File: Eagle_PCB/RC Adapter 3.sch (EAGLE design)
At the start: 20 parts, among them IC1 DRV8833, IC2 DRV8833, IC3 ARDUINO_PRO_MICRO, X1 MKDSN1,5/2-5,08

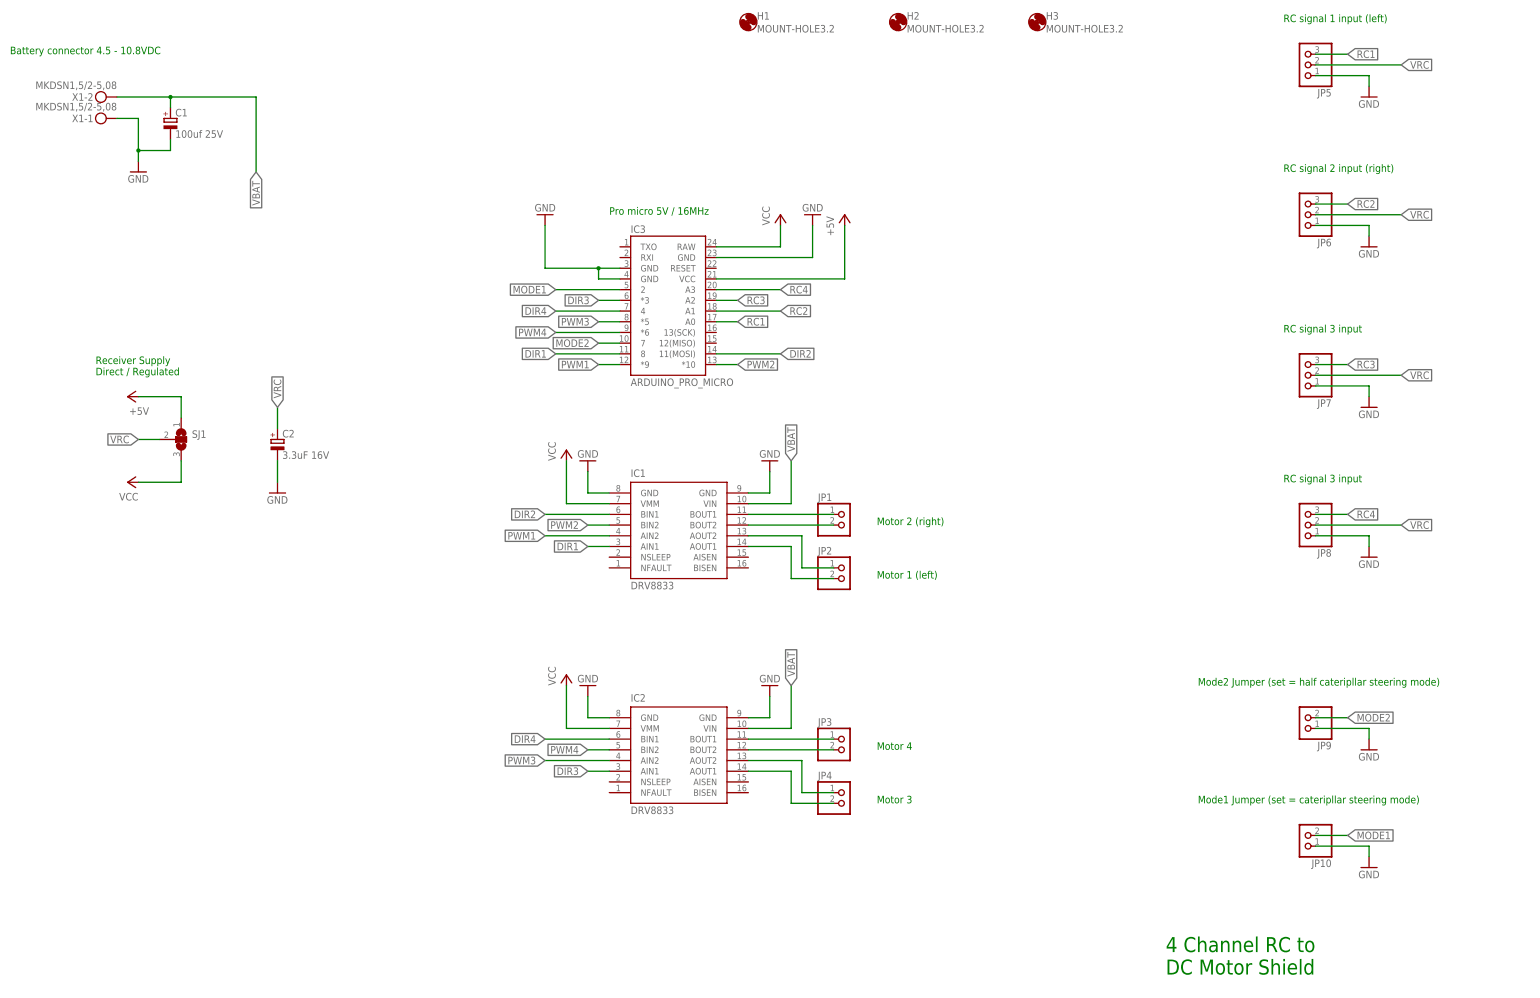
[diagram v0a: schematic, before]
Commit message: Updated to V1.1
Now also compatible with a Pro Mini
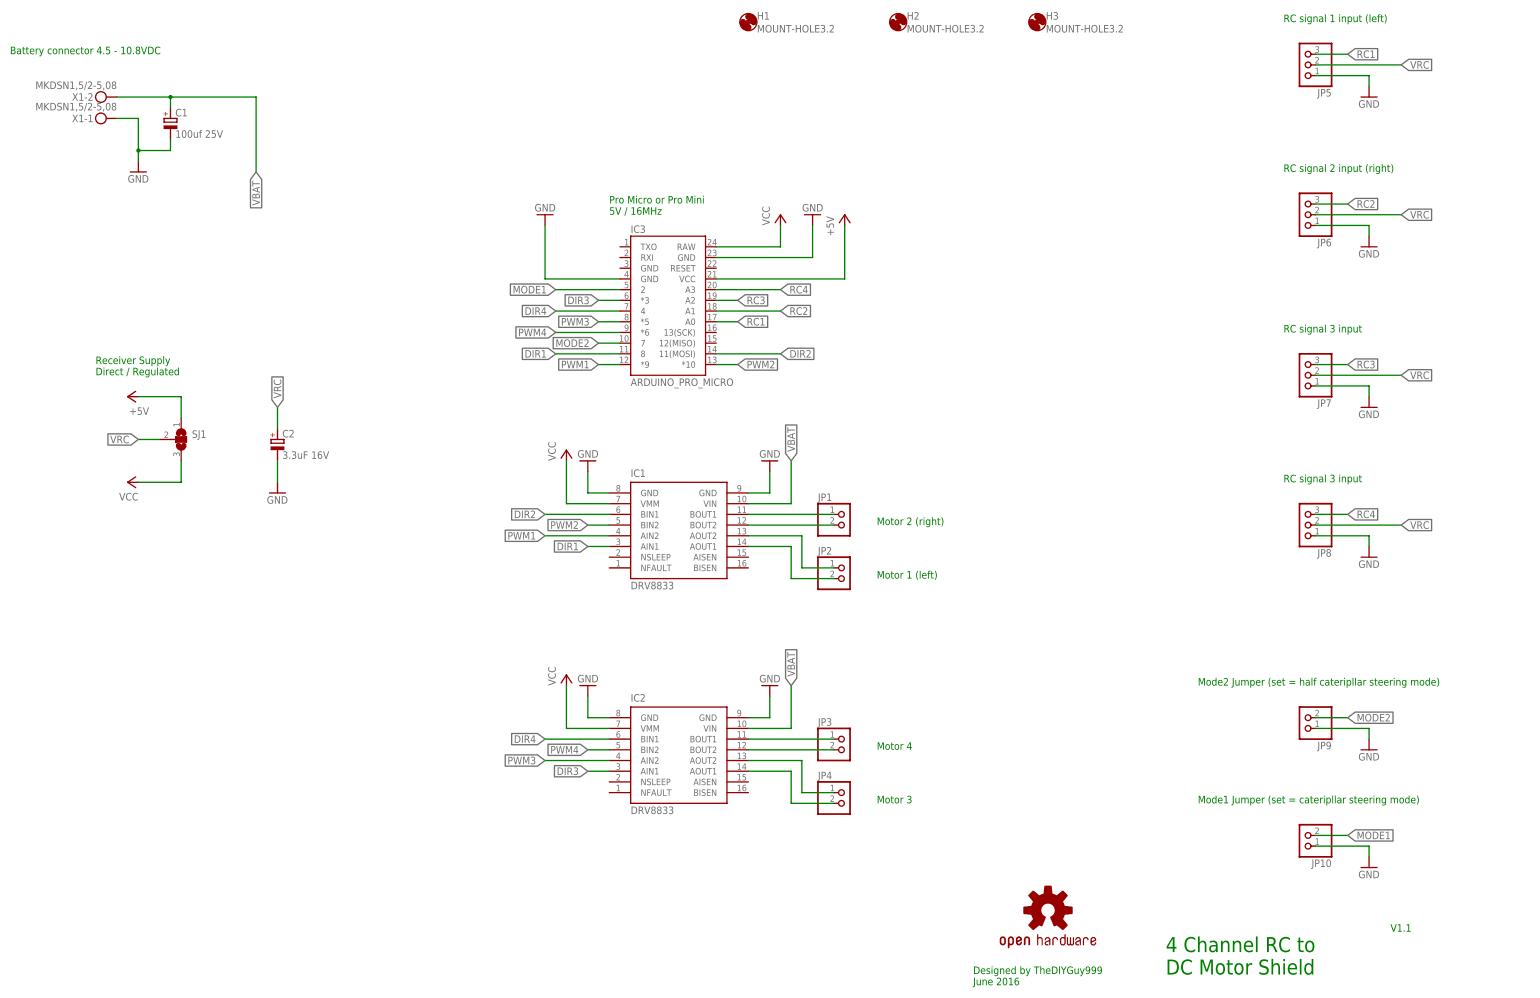
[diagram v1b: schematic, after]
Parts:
- added LOGO1: OSHW-LOGOL, SparkFun-Aesthetics:OSHW-LOGOL
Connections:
- net GND: no longer IC3.GND@1
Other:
- note added: "Designed by TheDIYGuy999 June 2016"
- note added: "Pro Micro or Pro Mini 5V / 16MHz"
- note added: "V1.1"
- note removed: "Pro micro 5V / 16MHz"
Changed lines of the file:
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@@
 <setting verticaltext="up"/>
 </settings>
-<grid distance="0.1" unitdist="inch" unit="inch" style="lines" multiple="1" display="yes" altdistance="0.01" altunitdist="inch" altunit="inch"/>
+<grid distance="0.1" unitdist="inch" unit="inch" style="lines" multiple="1" display="no" altdistance="0.01" altunitdist="inch" altunit="inch"/>
 <layers>
 <layer number="1" name="Top" color="4" fill="1" visible="no" active="no"/>
@@
 <part name="C2" library="rcl" deviceset="CPOL-EU" device="ETR1" value="3.3uF 16V"/>
 <part name="GND3" library="supply1" deviceset="GND" device=""/>
+<part name="LOGO1" library="SparkFun-Aesthetics" deviceset="OSHW-LOGO" device="L"/>
 </parts>
 <sheets>
 <sheet>
 <plain>
-<text x="160.02" y="190.5" size="1.778" layer="91">Pro micro 5V / 16MHz</text>
+<text x="160.02" y="190.5" size="1.778" layer="91">Pro Micro or Pro Mini
+5V / 16MHz</text>
 <text x="299.72" y="50.8" size="1.778" layer="91">Mode1 Jumper (set = cateripllar steering mode)</text>
 <text x="320.04" y="236.22" size="1.778" layer="91">RC signal 1 input (left)</text>
@@
 <text x="38.1" y="152.4" size="1.778" layer="91">Receiver Supply
 Direct / Regulated</text>
+<text x="345.44" y="20.32" size="1.778" layer="91">V1.1</text>
+<text x="246.38" y="7.62" size="1.778" layer="91">Designed by TheDIYGuy999
+June 2016</text>
 </plain>
 <instances>
@@
 <instance part="C2" gate="G$1" x="81.28" y="137.16"/>
 <instance part="GND3" gate="1" x="81.28" y="124.46"/>
+<instance part="LOGO1" gate="G$1" x="264.16" y="25.4"/>
 </instances>
 <busses>
@@
 <segment>
 <pinref part="GND1" gate="1" pin="GND"/>
-<pinref part="IC3" gate="G$1" pin="GND@1"/>
-<wire x1="144.78" y1="187.96" x2="144.78" y2="177.8" width="0.1524" layer="91"/>
-<wire x1="144.78" y1="177.8" x2="157.48" y2="177.8" width="0.1524" layer="91"/>
+<wire x1="144.78" y1="187.96" x2="144.78" y2="175.26" width="0.1524" layer="91"/>
 <pinref part="IC3" gate="G$1" pin="GND"/>
-<wire x1="157.48" y1="177.8" x2="162.56" y2="177.8" width="0.1524" layer="91"/>
-<wire x1="162.56" y1="175.26" x2="157.48" y2="175.26" width="0.1524" layer="91"/>
-<wire x1="157.48" y1="175.26" x2="157.48" y2="177.8" width="0.1524" layer="91"/>
-<junction x="157.48" y="177.8"/>
+<wire x1="162.56" y1="175.26" x2="144.78" y2="175.26" width="0.1524" layer="91"/>
 </segment>
 <segment>
